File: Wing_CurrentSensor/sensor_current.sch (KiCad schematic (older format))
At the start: 18 parts, among them U1 TL084, U2 AD8226

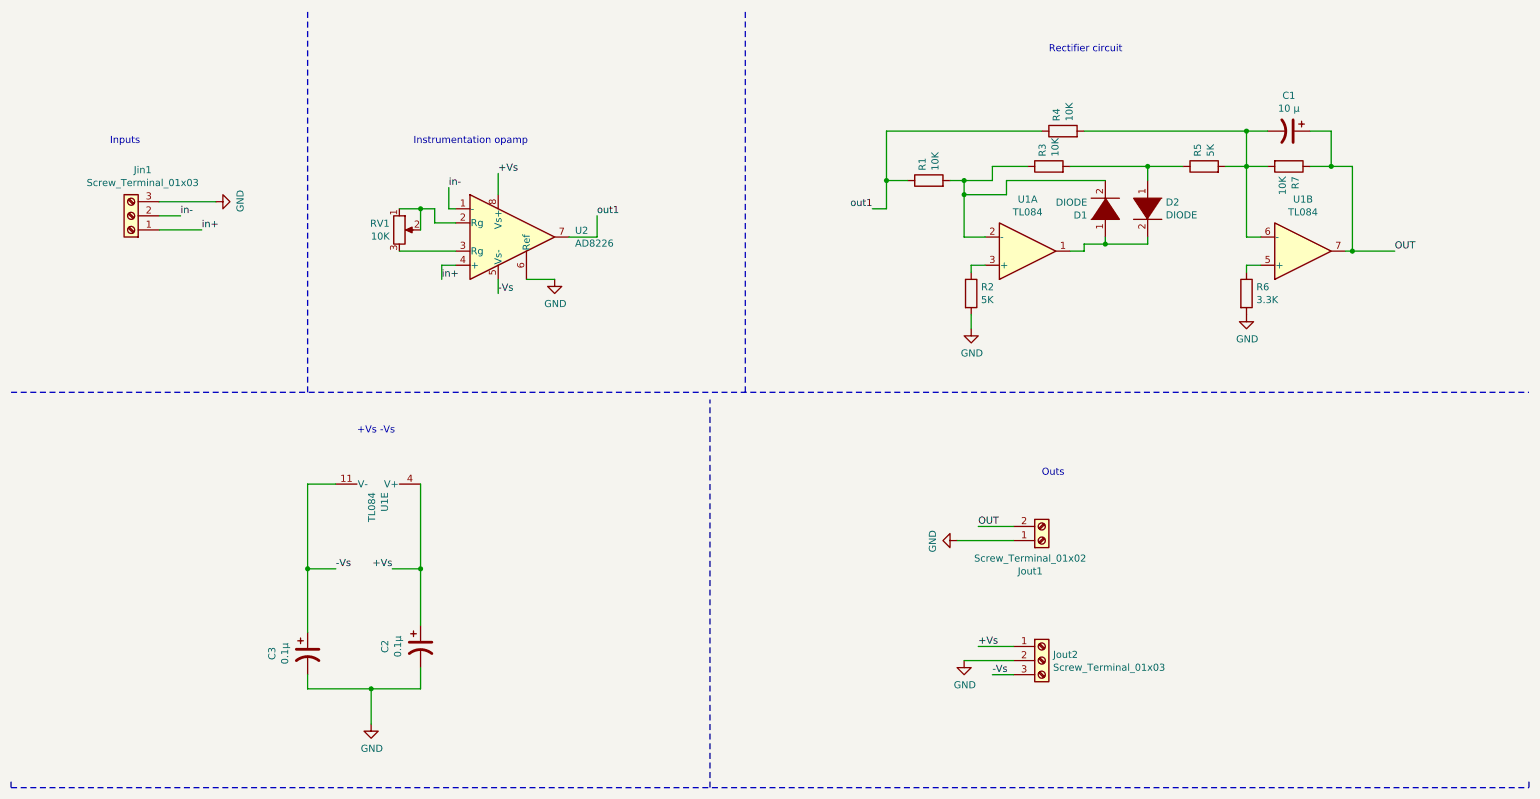
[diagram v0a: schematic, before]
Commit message: AD8226 eliminated
auto_awesome
Se muestra la traducción de se reemplazo el AD8226 por un modulo del TL084, ademas se cambio el orden de los modulos, siendo estos el modulo B,C y D, se realizo nuevo esquematico y nueva PCB del circuito
Traducir se remplazo el AD8226 por un modulo del TL084, ademas se cambio el orden de los modulos, siendo estos el modulo B,C y D, se realizo nuevo esquematico y nueva PCB del circuito
174 / 5000
Resultados de traducción
The AD8226 was replaced by a TL084 module, also the order of the modules was changed, these being module B, C and D, a new schematic and new circuit PCB was made
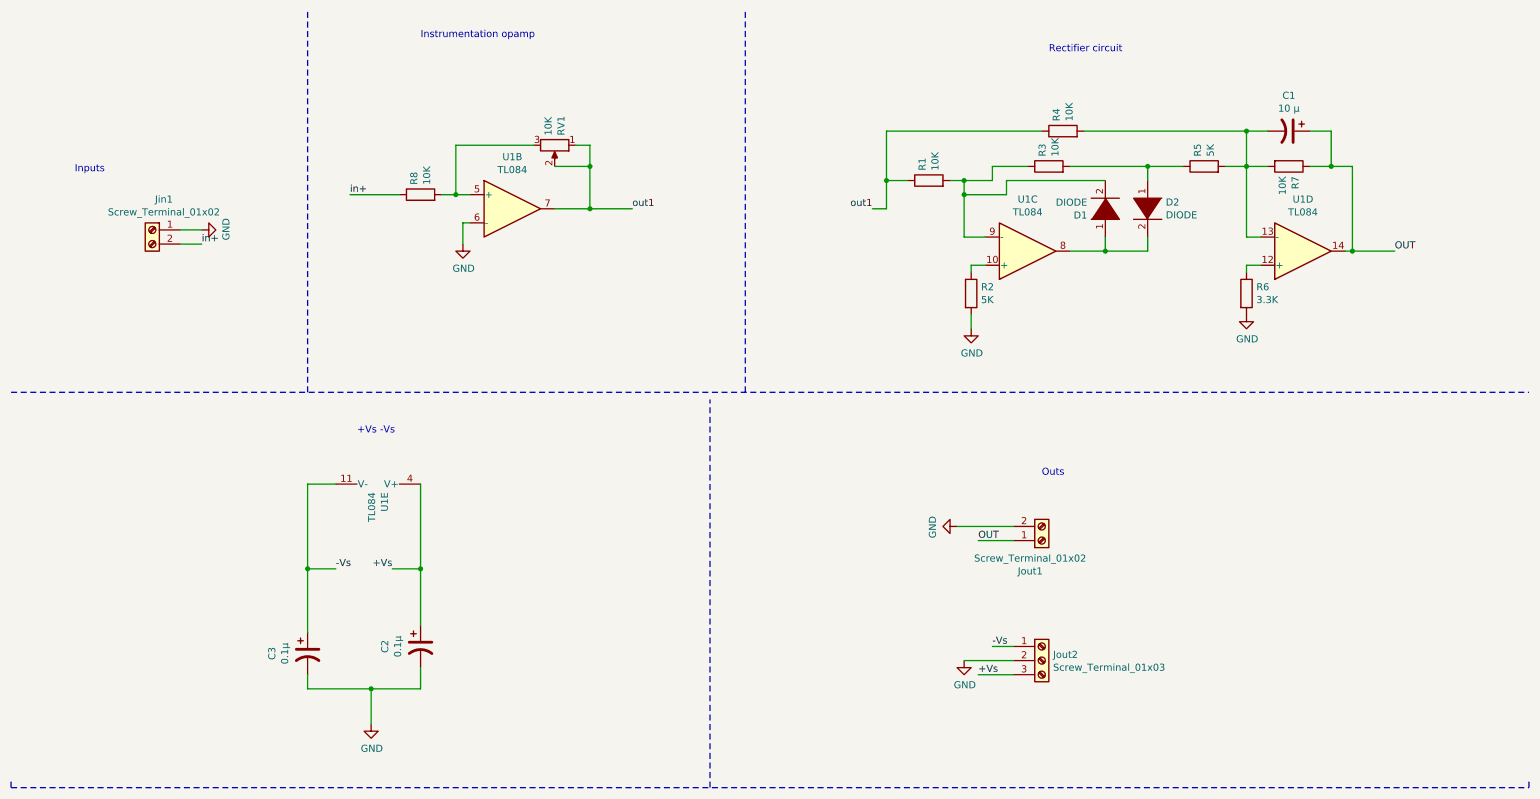
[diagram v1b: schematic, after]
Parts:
- removed Jin1: Screw_Terminal_01x03, TerminalBlock:TerminalBlock_Altech_AK300-3_P5.00mm, symbol Connector:Screw_Terminal_01x03
- removed unit 1 of U1
- removed U2: AD8226, Package_SO:SOIC-8_3.9x4.9mm_P1.27mm, symbol Amplifier_Instrumentation:AD8421
- added Jin1: Screw_Terminal_01x02, TerminalBlock:TerminalBlock_Altech_AK300-2_P5.00mm, symbol Connector:Screw_Terminal_01x02
- added R8: 10K, Resistor_SMD:R_0805_2012Metric_Pad1.20x1.40mm_HandSolder, symbol Device:R
- added unit 3 of U1
- added unit 4 of U1
- U1: footprint Package_SO:SO-14_3.9x8.65mm_P1.27mm -> (none)
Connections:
- net +Vs: now also Jout2.3 (Pin_3); no longer Jout2.1 (Pin_1)
- net -Vs: now also Jout2.1 (Pin_1); no longer Jout2.3 (Pin_3)
- net GND: now also Jout1.2 (Pin_2), U1.6 (-), Jin1.1 (Pin_1); no longer Jout1.1 (Pin_1)
- net OUT: now also Jout1.1 (Pin_1), U1.14; no longer Jout1.2 (Pin_2), U1.7
- net in+: now also Jin1.2 (Pin_2), R8.1
- net out1: now also RV1.1, RV1.2, U1.7
- net at RV1.3: now also U1.5 (+), R8.2
- net at R2.1: now also U1.10 (+)
- net at D1.1 (K), D2.2 (A): now also U1.8
- net at D1.2 (A), R1.2, R3.1: now also U1.9 (-)
- net at R6.1: now also U1.12 (+); no longer U1.5 (+)
- net at C1.2, R4.2, R5.2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: now also U1.13 (-); no longer U1.6 (-)

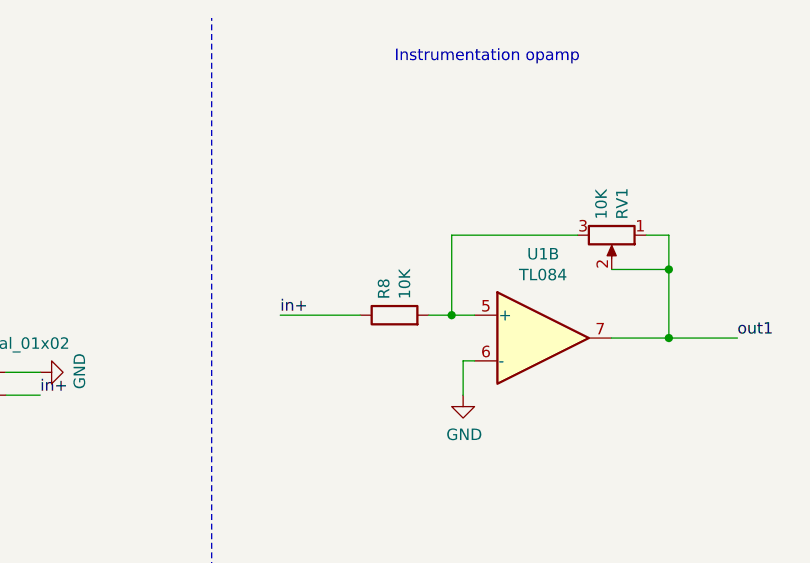
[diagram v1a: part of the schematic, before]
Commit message: Printable of PCB without AD8226
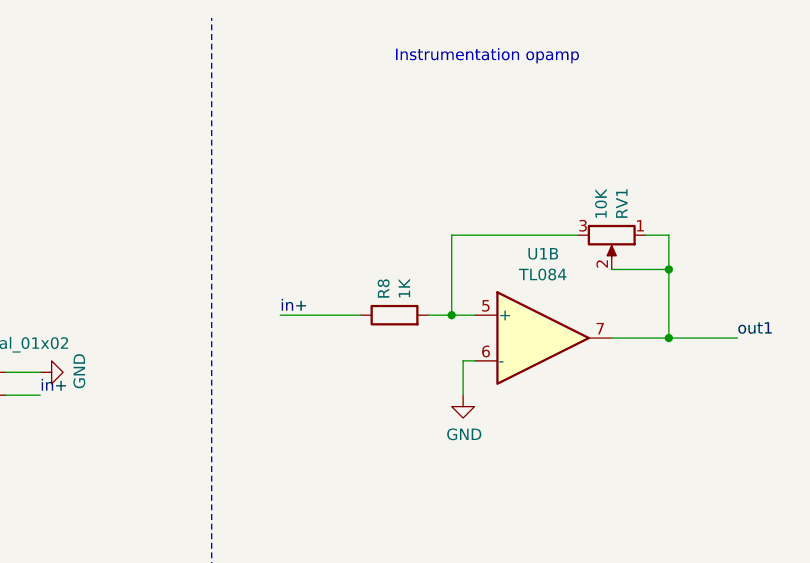
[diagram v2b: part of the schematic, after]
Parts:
- R8: value 10K -> 1K
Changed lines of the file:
@@
 P 3350 1750
 F 0 "R8" H 3420 1796 50  0000 L CNN
-F 1 "10K" H 3420 1705 50  0000 L CNN
+F 1 "1K" H 3420 1705 50  0000 L CNN
 F 2 "Resistor_SMD:R_0805_2012Metric_Pad1.20x1.40mm_HandSolder" V 3280 1750 50  0001 C CNN
 F 3 "~" H 3350 1750 50  0001 C CNN

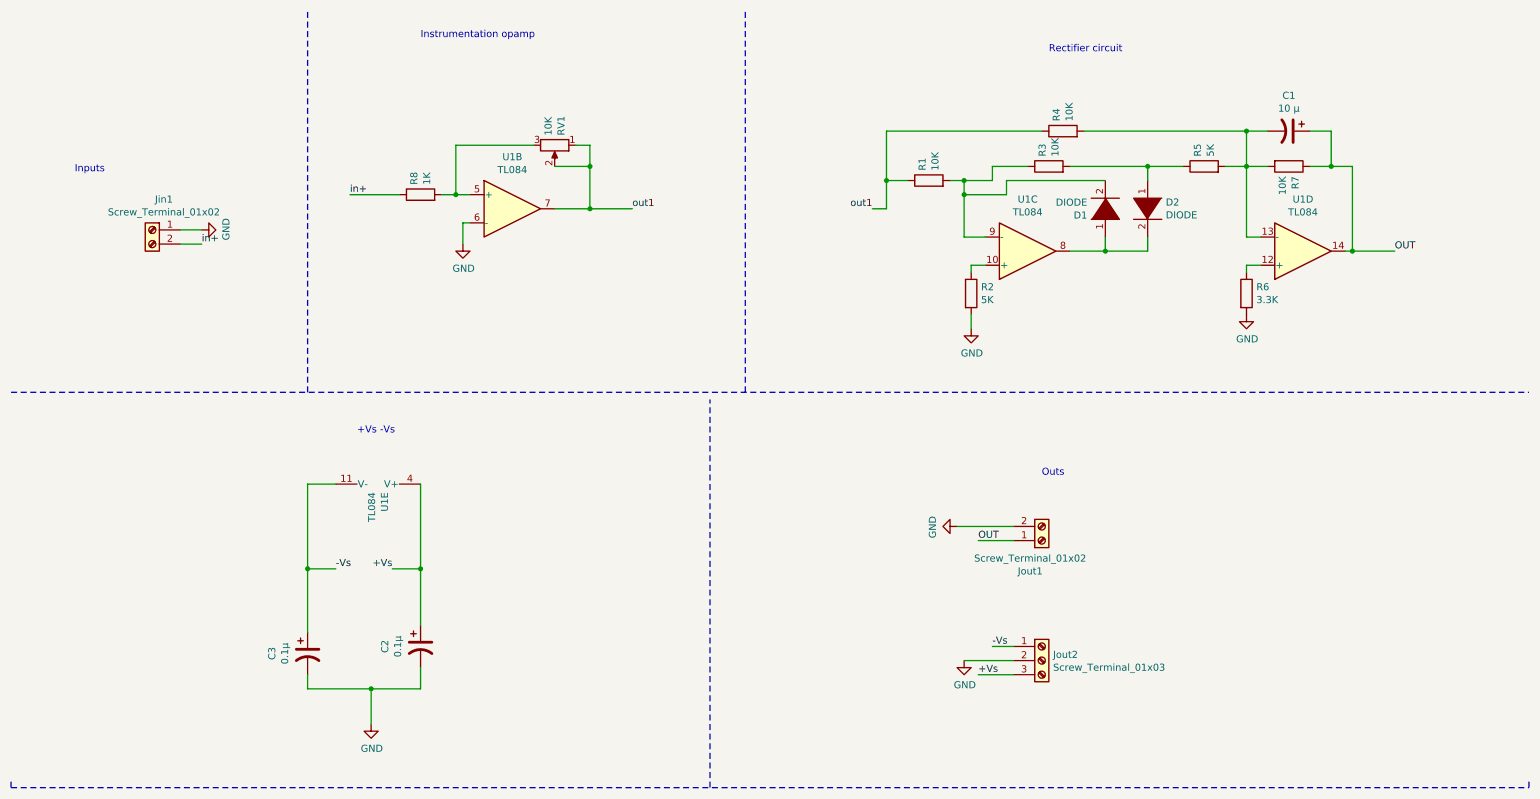
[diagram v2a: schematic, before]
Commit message: Manual version
1rst version of the PCB ad8226 and TL084
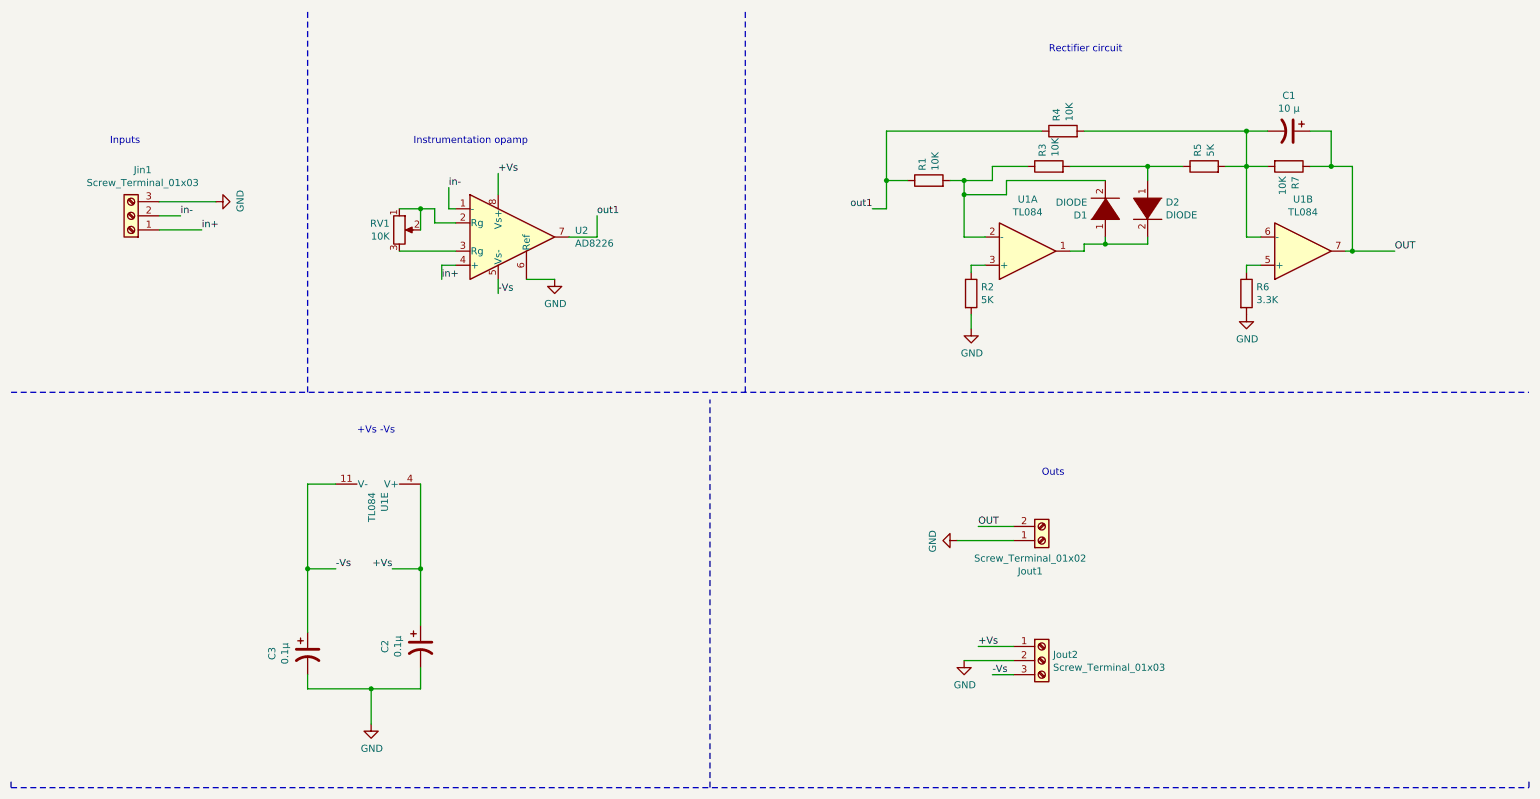
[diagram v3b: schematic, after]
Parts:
- removed Jin1: Screw_Terminal_01x02, TerminalBlock:TerminalBlock_Altech_AK300-2_P5.00mm, symbol Connector:Screw_Terminal_01x02
- removed R8: 1K, Resistor_SMD:R_0805_2012Metric_Pad1.20x1.40mm_HandSolder, symbol Device:R
- removed unit 3 of U1
- removed unit 4 of U1
- added Jin1: Screw_Terminal_01x03, TerminalBlock:TerminalBlock_Altech_AK300-3_P5.00mm, symbol Connector:Screw_Terminal_01x03
- added unit 1 of U1
- added U2: AD8226, Package_SO:SOIC-8_3.9x4.9mm_P1.27mm, symbol Amplifier_Instrumentation:AD8421
- U1: footprint (none) -> Package_SO:SO-14_3.9x8.65mm_P1.27mm
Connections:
- net +Vs: now also Jout2.1 (Pin_1), U2.8 (Vs+); no longer Jout2.3 (Pin_3)
- net -Vs: now also Jout2.3 (Pin_3), U2.5 (Vs-); no longer Jout2.1 (Pin_1)
- net GND: now also Jout1.1 (Pin_1), Jin1.3 (Pin_3), U2.6 (Ref); no longer Jout1.2 (Pin_2), U1.6 (-)
- net OUT: now also Jout1.2 (Pin_2), U1.7; no longer Jout1.1 (Pin_1)
- net in+: now also Jin1.1 (Pin_1), U2.4 (+)
- net out1: now also U2.7; no longer RV1.1, RV1.2, U1.7
- net at RV1.3: now also U2.3 (Rg); no longer U1.5 (+)
- net at R2.1: now also U1.3 (+)
- net at D1.1 (K), D2.2 (A): now also U1.1
- net at D1.2 (A), R1.2, R3.1: now also U1.2 (-)
- net at R6.1: now also U1.5 (+)
- net at C1.2, R4.2, R5.2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: now also U1.6 (-)
- new net: RV1.1, RV1.2, U2.2 (Rg)
- new net in-: Jin1.2 (Pin_2), U2.1 (-)
